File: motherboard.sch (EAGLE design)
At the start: 23 parts, among them U1 MC34063DIP

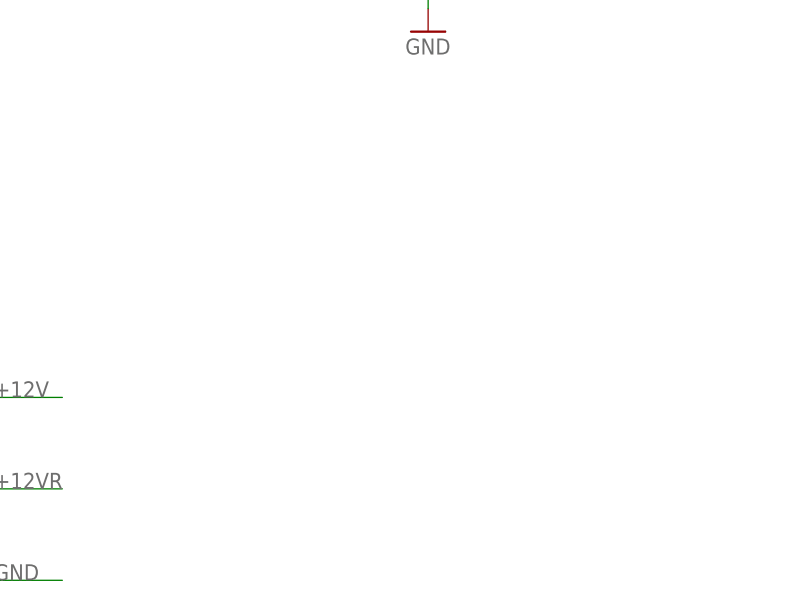
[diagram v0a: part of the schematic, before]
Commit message: Added 3.3v regulator and circuit
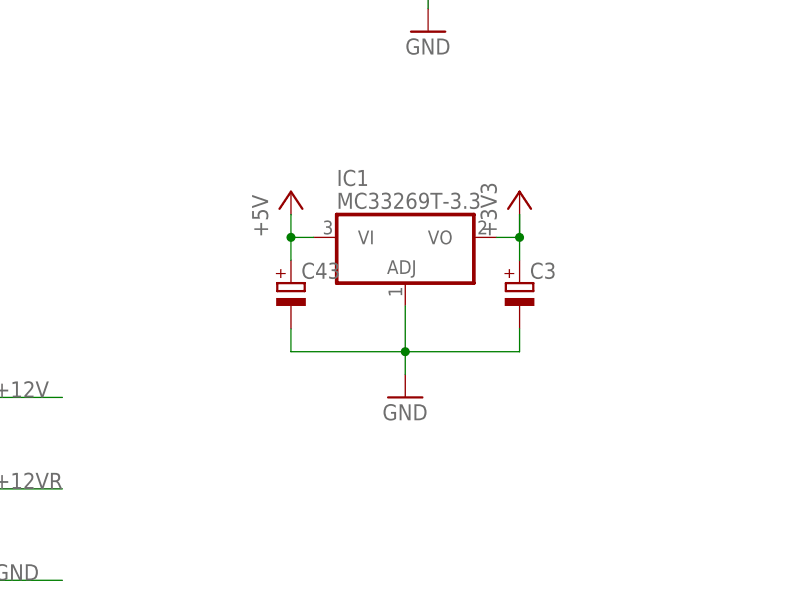
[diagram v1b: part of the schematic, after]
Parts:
- added C3, C43: (no value), rcl:CPOL-EUE2-4
- added IC1: MC33269T-3.3, linear:MC33269T-3.3
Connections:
- net +3V3: now also C3.+, IC1.VO
- net +5V: now also C43.+, IC1.VI
- net GND: now also C3.-, C43.-, IC1.ADJ
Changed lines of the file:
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@@
 <part name="P+25" library="supply1" deviceset="+5V" device=""/>
 <part name="GND27" library="supply1" deviceset="GND" device=""/>
+<part name="IC1" library="linear" deviceset="MC33269?*" device="T" technology="-3.3"/>
+<part name="+3V2" library="supply1" deviceset="+3V3" device=""/>
+<part name="P+2" library="supply1" deviceset="+5V" device=""/>
+<part name="GND2" library="supply1" deviceset="GND" device=""/>
+<part name="C3" library="rcl" deviceset="CPOL-EU" device="E2-4"/>
+<part name="C43" library="rcl" deviceset="CPOL-EU" device="E2-4"/>
 </parts>
 <sheets>
@@
 <instance part="P+25" gate="1" x="104.14" y="50.8"/>
 <instance part="GND27" gate="1" x="104.14" y="33.02"/>
+<instance part="IC1" gate="G$1" x="137.16" y="0"/>
+<instance part="+3V2" gate="G$1" x="149.86" y="7.62"/>
+<instance part="P+2" gate="1" x="124.46" y="7.62"/>
+<instance part="GND2" gate="1" x="137.16" y="-15.24"/>
+<instance part="C3" gate="G$1" x="149.86" y="-2.54"/>
+<instance part="C43" gate="G$1" x="124.46" y="-2.54"/>
 </instances>
 <busses>
@@
 <wire x1="104.14" y1="35.56" x2="104.14" y2="38.1" width="0.1524" layer="91"/>
 </segment>
+<segment>
+<pinref part="GND2" gate="1" pin="GND"/>
+<pinref part="IC1" gate="G$1" pin="ADJ"/>
+<wire x1="137.16" y1="-12.7" x2="137.16" y2="-10.16" width="0.1524" layer="91"/>
+<pinref part="C43" gate="G$1" pin="-"/>
+<wire x1="137.16" y1="-10.16" x2="137.16" y2="-5.08" width="0.1524" layer="91"/>
+<wire x1="137.16" y1="-10.16" x2="124.46" y2="-10.16" width="0.1524" layer="91"/>
+<wire x1="124.46" y1="-10.16" x2="124.46" y2="-7.62" width="0.1524" layer="91"/>
+<pinref part="C3" gate="G$1" pin="-"/>
+<wire x1="137.16" y1="-10.16" x2="149.86" y2="-10.16" width="0.1524" layer="91"/>
+<wire x1="149.86" y1="-10.16" x2="149.86" y2="-7.62" width="0.1524" layer="91"/>
+<junction x="137.16" y="-10.16"/>
+</segment>
 </net>
 <net name="+3V3" class="0">
@@
 <junction x="48.26" y="71.12"/>
 </segment>
+<segment>
+<pinref part="IC1" gate="G$1" pin="VO"/>
+<wire x1="147.32" y1="2.54" x2="149.86" y2="2.54" width="0.1524" layer="91"/>
+<pinref part="+3V2" gate="G$1" pin="+3V3"/>
+<wire x1="149.86" y1="2.54" x2="149.86" y2="5.08" width="0.1524" layer="91"/>
+<wire x1="149.86" y1="5.08" x2="149.86" y2="2.54" width="0.1524" layer="91"/>
+<pinref part="C3" gate="G$1" pin="+"/>
+<junction x="149.86" y="2.54"/>
+<wire x1="149.86" y1="2.54" x2="149.86" y2="0" width="0.1524" layer="91"/>
+</segment>
 </net>
 <net name="+5V" class="0">
@@
 <wire x1="104.14" y1="45.72" x2="104.14" y2="48.26" width="0.1524" layer="91"/>
 </segment>
-</net>
+<segment>
+<pinref part="P+2" gate="1" pin="+5V"/>
+<wire x1="124.46" y1="5.08" x2="124.46" y2="2.54" width="0.1524" layer="91"/>
+<pinref part="IC1" gate="G$1" pin="VI"/>
+<wire x1="127" y1="2.54" x2="124.46" y2="2.54" width="0.1524" layer="91"/>
+<wire x1="124.46" y1="2.54" x2="124.46" y2="0" width="0.1524" layer="91"/>
+<pinref part="C43" gate="G$1" pin="+"/>
+<junction x="124.46" y="2.54"/>
+</segment>
+</net>
